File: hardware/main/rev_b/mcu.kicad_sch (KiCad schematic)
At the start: 23 parts, among them J10 SWD, U10 RP2354B, Y1 12MHz ABM8-272-T3

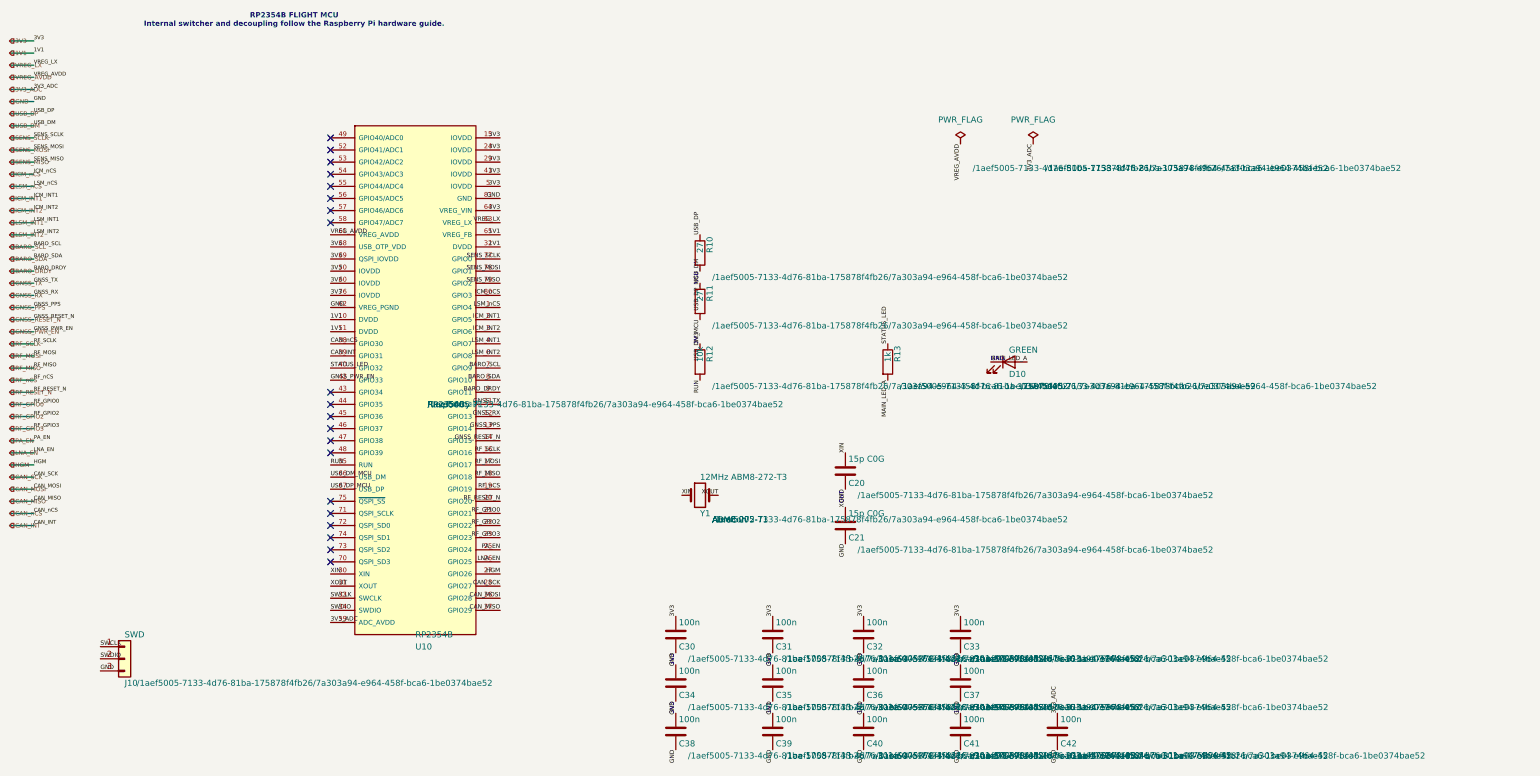
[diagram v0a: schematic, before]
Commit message: fix: consolidate portable Rev-B hardware sources
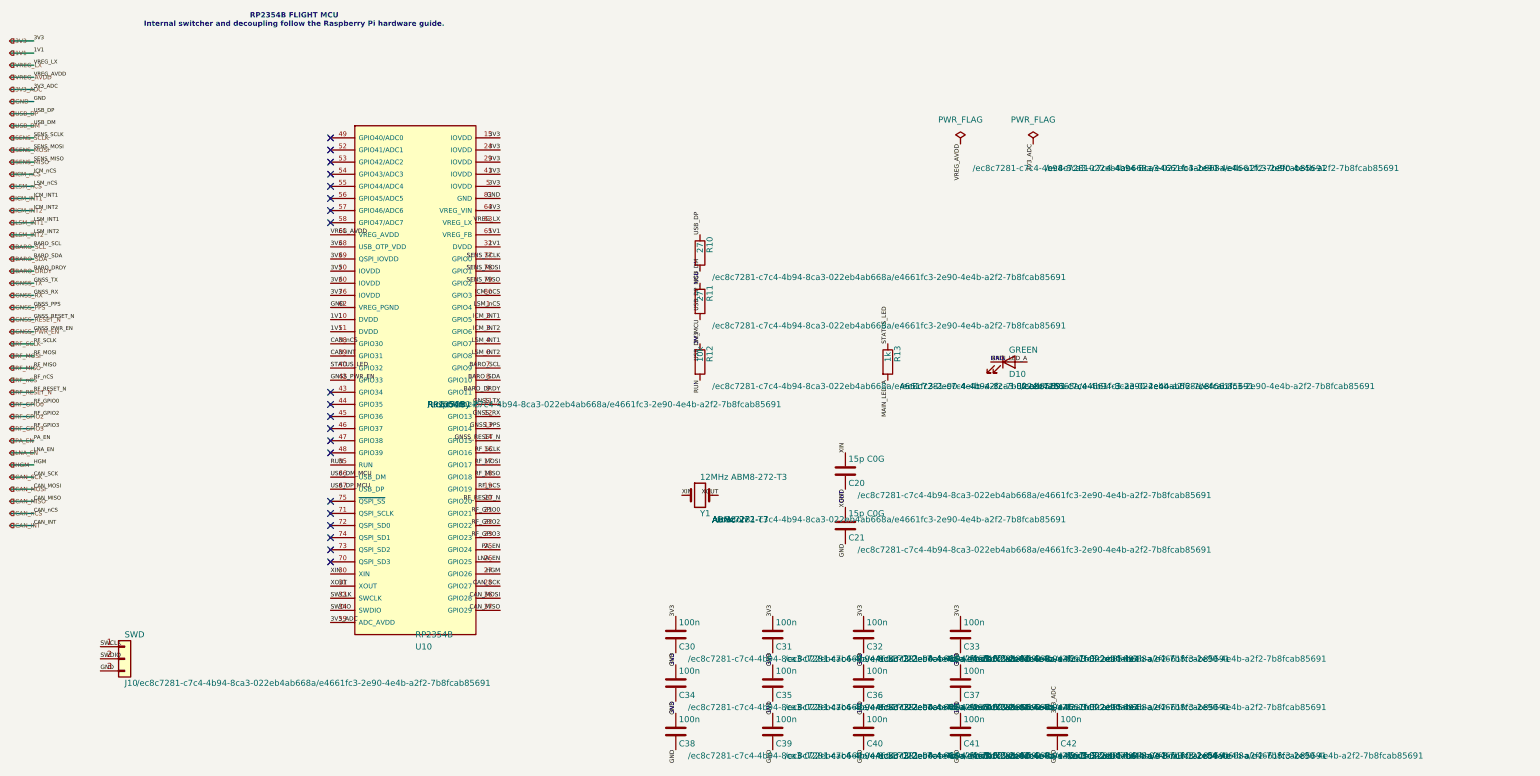
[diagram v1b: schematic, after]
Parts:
- C20, C21, C30, C31, C32, C33, C34, C35, C36, C37, C38, C39, C40, C41, C42, D10, J10, R10, R11, R12, R13, U10, Y1: hierarchy_path /1aef5005-7133-4d76-81ba-175878f4fb26/7a303a94-e964-458f-bc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 -> /ec8c7281-c7c4-4b94-8ca3-022eb4ab668a/e4661fc3-2e90-4e4b-a2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
